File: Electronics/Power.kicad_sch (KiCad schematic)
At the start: 67 parts, among them IC1 TPS65251-1RHAR, IC2 MAX20008AFOC_VY+T, U6 AMS1117-3.3

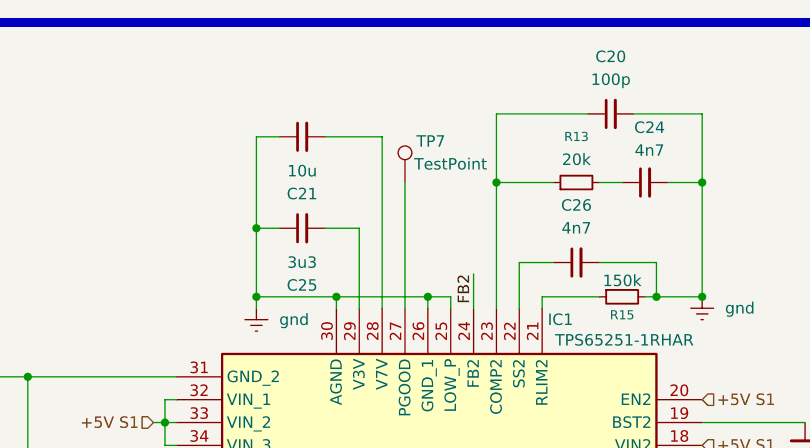
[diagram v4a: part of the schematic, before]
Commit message: Sata Port Changed
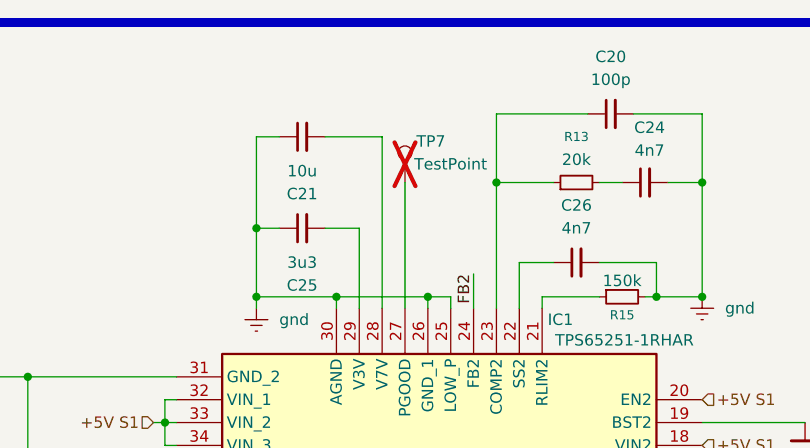
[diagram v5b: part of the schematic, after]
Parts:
- TP7: now not fitted; now left out of the parts list
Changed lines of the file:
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@@
 		(dnp no)
 		(fields_autoplaced yes)
-		(property "Reference" "#PWR050"
+		(property "Reference" "#PWR051"
 			(at 68.58 120.65 0)
 			(effects
@@
 			(project "CM5 Nas"
 				(path "/0650c7a8-acba-429c-9f8e-eec0baf0bc1c/fede4c36-00cc-4d3d-b71c-5243ba232202/588cd356-21c7-4636-b12c-e09ccb478c44"
-					(reference "#PWR050")
+					(reference "#PWR051")
 					(unit 1)
 				)
@@
 		(dnp no)
 		(fields_autoplaced yes)
-		(property "Reference" "#PWR040"
+		(property "Reference" "#PWR041"
 			(at 77.47 54.61 0)
 			(effects
@@
 			(project "CM5 Nas"
 				(path "/0650c7a8-acba-429c-9f8e-eec0baf0bc1c/fede4c36-00cc-4d3d-b71c-5243ba232202/588cd356-21c7-4636-b12c-e09ccb478c44"
-					(reference "#PWR040")
+					(reference "#PWR041")
 					(unit 1)
 				)
@@
 		(dnp no)
 		(fields_autoplaced yes)
-		(property "Reference" "#PWR043"
+		(property "Reference" "#PWR044"
 			(at 219.71 74.93 0)
 			(effects
@@
 			(project "CM5 Nas"
 				(path "/0650c7a8-acba-429c-9f8e-eec0baf0bc1c/fede4c36-00cc-4d3d-b71c-5243ba232202/588cd356-21c7-4636-b12c-e09ccb478c44"
-					(reference "#PWR043")
+					(reference "#PWR044")
 					(unit 1)
 				)
@@
 		(dnp no)
 		(fields_autoplaced yes)
-		(property "Reference" "#PWR039"
+		(property "Reference" "#PWR040"
 			(at 127 53.34 0)
 			(effects
@@
 			(project "CM5 Nas"
 				(path "/0650c7a8-acba-429c-9f8e-eec0baf0bc1c/fede4c36-00cc-4d3d-b71c-5243ba232202/588cd356-21c7-4636-b12c-e09ccb478c44"
-					(reference "#PWR039")
+					(reference "#PWR040")
 					(unit 1)
 				)
@@
 		(dnp no)
 		(fields_autoplaced yes)
-		(property "Reference" "#PWR041"
+		(property "Reference" "#PWR042"
 			(at 41.91 63.5 0)
 			(effects
@@
 			(project ""
 				(path "/0650c7a8-acba-429c-9f8e-eec0baf0bc1c/fede4c36-00cc-4d3d-b71c-5243ba232202/588cd356-21c7-4636-b12c-e09ccb478c44"
-					(reference "#PWR041")
+					(reference "#PWR042")
 					(unit 1)
 				)
@@
 		(dnp no)
 		(fields_autoplaced yes)
-		(property "Reference" "#PWR042"
+		(property "Reference" "#PWR043"
 			(at 152.4 50.8 0)
 			(effects
@@
 			(project "CM5 Nas"
 				(path "/0650c7a8-acba-429c-9f8e-eec0baf0bc1c/fede4c36-00cc-4d3d-b71c-5243ba232202/588cd356-21c7-4636-b12c-e09ccb478c44"
-					(reference "#PWR042")
+					(reference "#PWR043")
 					(unit 1)
 				)
@@
 		(on_board yes)
 		(dnp no)
-		(property "Reference" "#PWR051"
+		(property "Reference" "#PWR052"
 			(at 127 120.65 0)
 			(effects
@@
 			(project "CM5 Nas"
 				(path "/0650c7a8-acba-429c-9f8e-eec0baf0bc1c/fede4c36-00cc-4d3d-b71c-5243ba232202/588cd356-21c7-4636-b12c-e09ccb478c44"
-					(reference "#PWR051")
+					(reference "#PWR052")
 					(unit 1)
 				)
@@
 		(on_board yes)
 		(dnp no)
-		(property "Reference" "#PWR049"
+		(property "Reference" "#PWR050"
 			(at 251.46 109.22 0)
 			(effects
@@
 			(project "CM5 Nas"
 				(path "/0650c7a8-acba-429c-9f8e-eec0baf0bc1c/fede4c36-00cc-4d3d-b71c-5243ba232202/588cd356-21c7-4636-b12c-e09ccb478c44"
-					(reference "#PWR049")
+					(reference "#PWR050")
 					(unit 1)
 				)
@@
 		(dnp no)
 		(fields_autoplaced yes)
-		(property "Reference" "#PWR048"
+		(property "Reference" "#PWR049"
 			(at 99.06 107.95 0)
 			(effects
@@
 			(project "CM5 Nas"
 				(path "/0650c7a8-acba-429c-9f8e-eec0baf0bc1c/fede4c36-00cc-4d3d-b71c-5243ba232202/588cd356-21c7-4636-b12c-e09ccb478c44"
-					(reference "#PWR048")
+					(reference "#PWR049")
 					(unit 1)
 				)
@@
 		(dnp no)
 		(fields_autoplaced yes)
-		(property "Reference" "#PWR038"
+		(property "Reference" "#PWR039"
 			(at 165.1 30.48 0)
 			(effects
@@
 			(project "CM5 Nas"
 				(path "/0650c7a8-acba-429c-9f8e-eec0baf0bc1c/fede4c36-00cc-4d3d-b71c-5243ba232202/588cd356-21c7-4636-b12c-e09ccb478c44"
-					(reference "#PWR038")
+					(reference "#PWR039")
 					(unit 1)
 				)
@@
 		(on_board yes)
 		(dnp no)
-		(property "Reference" "#PWR0172"
+		(property "Reference" "#PWR035"
 			(at 29.21 31.75 0)
 			(effects
@@
 			(project "CM5 Nas"
 				(path "/0650c7a8-acba-429c-9f8e-eec0baf0bc1c/fede4c36-00cc-4d3d-b71c-5243ba232202/588cd356-21c7-4636-b12c-e09ccb478c44"
-					(reference "#PWR0172")
+					(reference "#PWR035")
 					(unit 1)
 				)
@@
 		(on_board yes)
 		(dnp no)
-		(property "Reference" "#PWR052"
+		(property "Reference" "#PWR053"
 			(at 226.06 128.27 0)
 			(effects
@@
 			(project "CM5 Nas"
 				(path "/0650c7a8-acba-429c-9f8e-eec0baf0bc1c/fede4c36-00cc-4d3d-b71c-5243ba232202/588cd356-21c7-4636-b12c-e09ccb478c44"
-					(reference "#PWR052")
+					(reference "#PWR053")
 					(unit 1)
 				)
@@
 		(unit 1)
 		(exclude_from_sim no)
-		(in_bom yes)
+		(in_bom no)
 		(on_board yes)
-		(dnp no)
+		(dnp yes)
 		(property "Reference" "TP7"
 			(at 95.25 29.718 0)
@@
 		(dnp no)
 		(fields_autoplaced yes)
-		(property "Reference" "#PWR046"
+		(property "Reference" "#PWR047"
 			(at 29.21 104.14 0)
 			(effects
@@
 			(project "CM5 Nas"
 				(path "/0650c7a8-acba-429c-9f8e-eec0baf0bc1c/fede4c36-00cc-4d3d-b71c-5243ba232202/588cd356-21c7-4636-b12c-e09ccb478c44"
-					(reference "#PWR046")
+					(reference "#PWR047")
 					(unit 1)
 				)
@@
 		(dnp no)
 		(fields_autoplaced yes)
-		(property "Reference" "#PWR045"
+		(property "Reference" "#PWR046"
 			(at 152.4 86.36 0)
 			(effects
@@
 			(project "CM5 Nas"
 				(path "/0650c7a8-acba-429c-9f8e-eec0baf0bc1c/fede4c36-00cc-4d3d-b71c-5243ba232202/588cd356-21c7-4636-b12c-e09ccb478c44"
-					(reference "#PWR045")
+					(reference "#PWR046")
 					(unit 1)
 				)
@@
 		(dnp no)
 		(fields_autoplaced yes)
-		(property "Reference" "#PWR047"
+		(property "Reference" "#PWR048"
 			(at 165.1 106.68 0)
 			(effects
@@
 			(project "CM5 Nas"
 				(path "/0650c7a8-acba-429c-9f8e-eec0baf0bc1c/fede4c36-00cc-4d3d-b71c-5243ba232202/588cd356-21c7-4636-b12c-e09ccb478c44"
-					(reference "#PWR047")
+					(reference "#PWR048")
 					(unit 1)
 				)
@@
 		(dnp no)
 		(fields_autoplaced yes)
-		(property "Reference" "#PWR044"
+		(property "Reference" "#PWR045"
 			(at 41.91 85.09 0)
 			(effects
@@
 			(project "CM5 Nas"
 				(path "/0650c7a8-acba-429c-9f8e-eec0baf0bc1c/fede4c36-00cc-4d3d-b71c-5243ba232202/588cd356-21c7-4636-b12c-e09ccb478c44"
-					(reference "#PWR044")
+					(reference "#PWR045")
 					(unit 1)
 				)
@@
 		(dnp no)
 		(fields_autoplaced yes)
-		(property "Reference" "#PWR036"
+		(property "Reference" "#PWR037"
 			(at 210.82 40.64 0)
 			(effects
@@
 			(project "CM5 Nas"
 				(path "/0650c7a8-acba-429c-9f8e-eec0baf0bc1c/fede4c36-00cc-4d3d-b71c-5243ba232202/588cd356-21c7-4636-b12c-e09ccb478c44"
-					(reference "#PWR036")
+					(reference "#PWR037")
 					(unit 1)
 				)
@@
 		(dnp no)
 		(fields_autoplaced yes)
-		(property "Reference" "#PWR035"
+		(property "Reference" "#PWR036"
 			(at 200.66 40.64 0)
 			(effects
@@
 			(project "CM5 Nas"
 				(path "/0650c7a8-acba-429c-9f8e-eec0baf0bc1c/fede4c36-00cc-4d3d-b71c-5243ba232202/588cd356-21c7-4636-b12c-e09ccb478c44"
-					(reference "#PWR035")
+					(reference "#PWR036")
 					(unit 1)
 				)
@@
 		(dnp no)
 		(fields_autoplaced yes)
-		(property "Reference" "#PWR037"
+		(property "Reference" "#PWR038"
 			(at 220.98 40.64 0)
 			(effects
@@
 			(project "CM5 Nas"
 				(path "/0650c7a8-acba-429c-9f8e-eec0baf0bc1c/fede4c36-00cc-4d3d-b71c-5243ba232202/588cd356-21c7-4636-b12c-e09ccb478c44"
-					(reference "#PWR037")
+					(reference "#PWR038")
 					(unit 1)
 				)

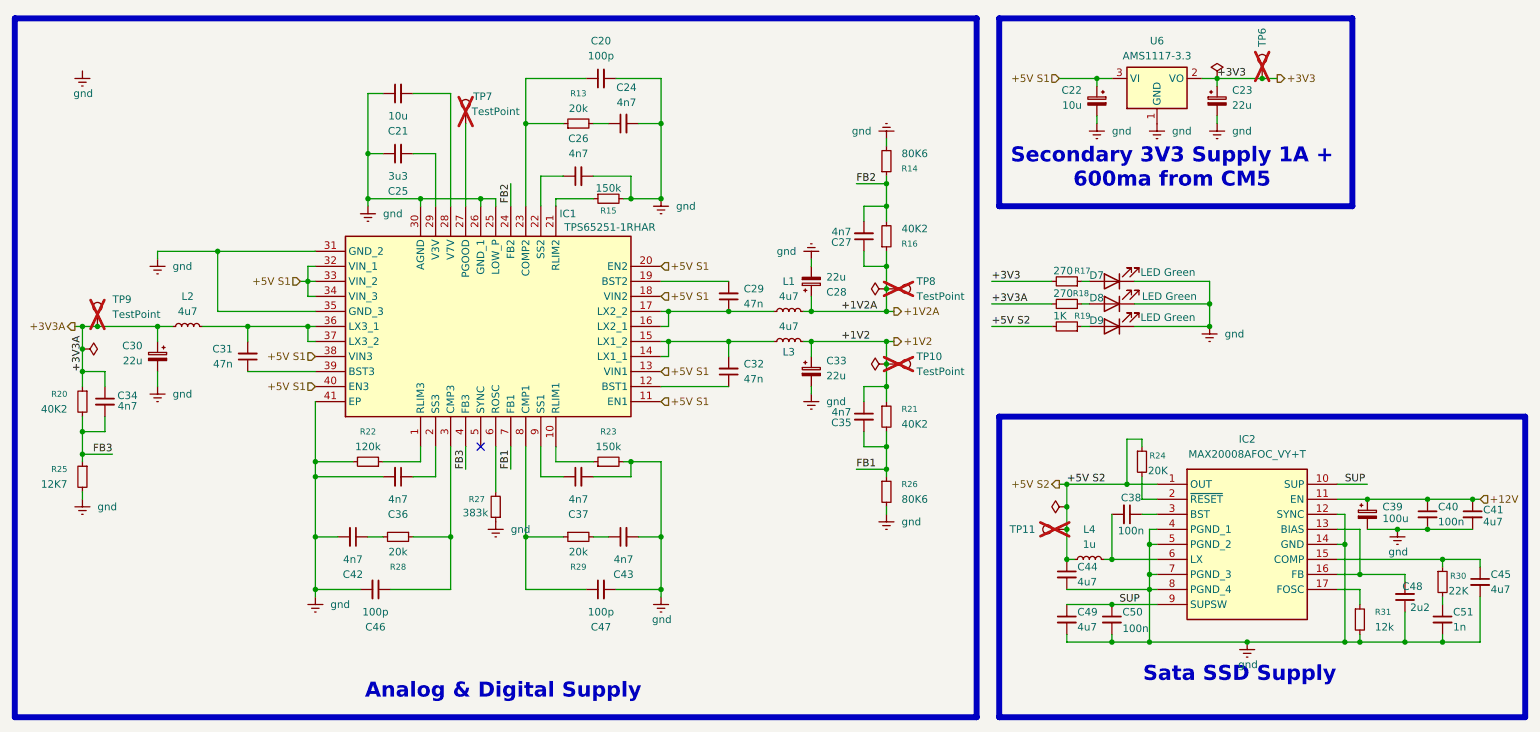
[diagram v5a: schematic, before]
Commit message: Changed sata port
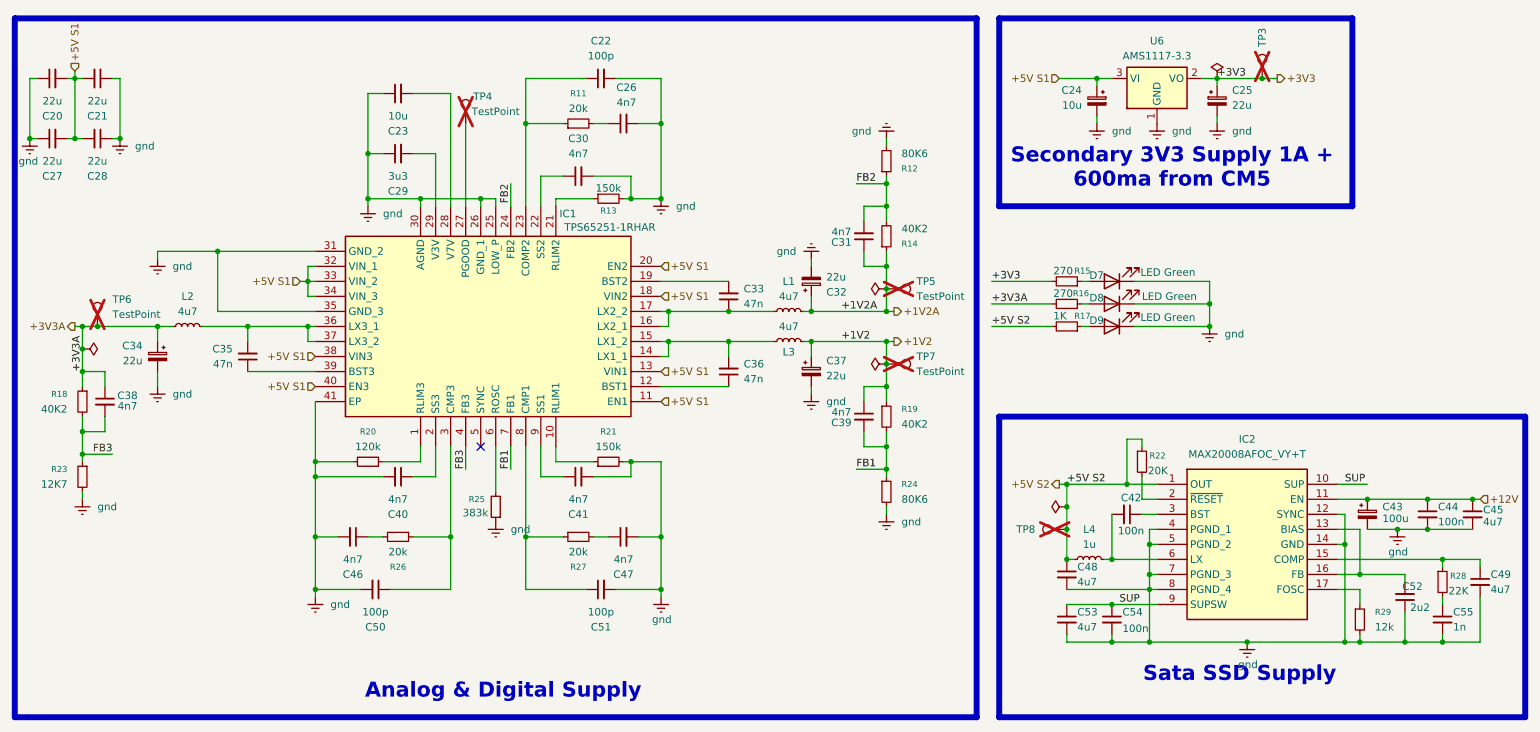
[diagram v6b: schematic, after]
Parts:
- added C20, C21, C27, C28: 22u, Capacitor_SMD:C_0805_2012Metric, symbol Device:C_Small
- IC1: footprint TPS65251-1RHAR:QFN50P600X600X100-41N-D -> Package_DFN_QFN:VQFN-40-1EP_6x6mm_P0.5mm_EP3.5x3.5mm_ThermalVias
- renumbered C20 to C22, C21 to C23, C22 to C24, C23 to C25, C24 to C26, C25 to C29, C26 to C30, C27 to C31, C28 to C32, C29 to C33, C30 to C34, C31 to C35, C32 to C36, C33 to C37, C34 to C38, C35 to C39, C36 to C40, C37 to C41, C38 to C42, C39 to C43, C40 to C44, C41 to C45, C42 to C46, C43 to C47, C44 to C48, C45 to C49, C46 to C50, C47 to C51, C48 to C52, C49 to C53, C50 to C54, C51 to C55, R13 to R11, R14 to R12, R15 to R13, R16 to R14, R17 to R15, R18 to R16, R19 to R17, R20 to R18, R21 to R19, R22 to R20, R23 to R21, R24 to R22, R25 to R23, R26 to R24, R27 to R25, R28 to R26, R29 to R27, R30 to R28, R31 to R29, TP6 to TP3, TP7 to TP4, TP8 to TP5, TP9 to TP6, TP10 to TP7, TP11 to TP8
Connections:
- net +5V S1: now also C20.2, C21.2, C27.2, C28.2
- net gnd: now also C20.1, C21.1, C27.1, C28.1

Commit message: More pcbing
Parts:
- removed C28: 22u, Capacitor_SMD:C_0805_2012Metric, symbol Device:C_Small
- C49, C53: footprint Capacitor_SMD:C_0805_2012Metric -> Capacitor_SMD:C_0402_1005Metric
- C52: footprint Capacitor_SMD:C_0603_1608Metric -> Capacitor_SMD:C_0402_1005Metric
- R18, R19, R23, R24, R25: footprint Resistor_SMD:R_0603_1608Metric -> Resistor_SMD:R_0402_1005Metric
- R28: footprint Resistor_SMD:R_0603_1608Metric -> Capacitor_SMD:C_0402_1005Metric
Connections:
- net SUP is gone; now on net +12V: C53.1, C54.1, IC2.10 (SUP), IC2.9 (SUPSW)

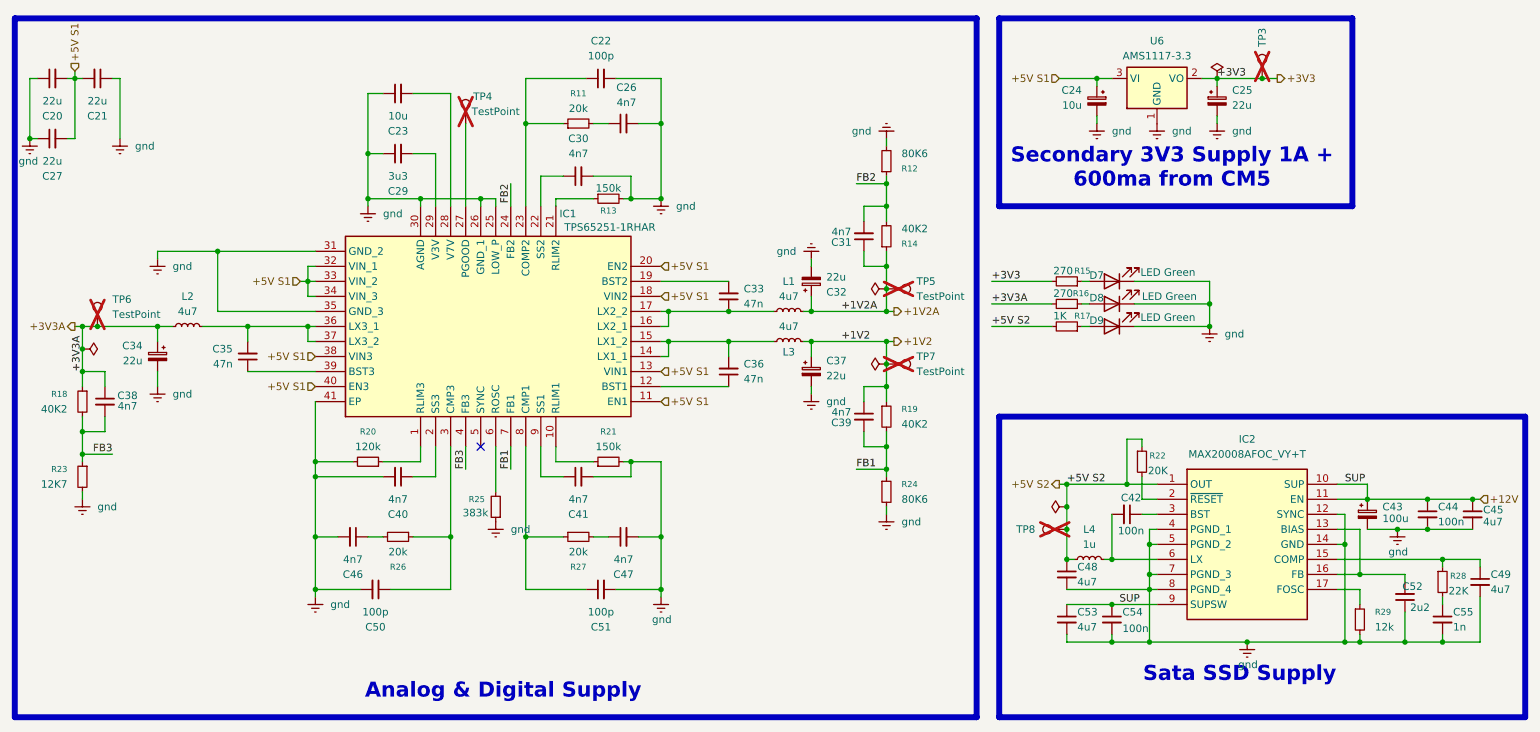
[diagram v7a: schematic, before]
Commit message: More pcb arangment, verticle ports
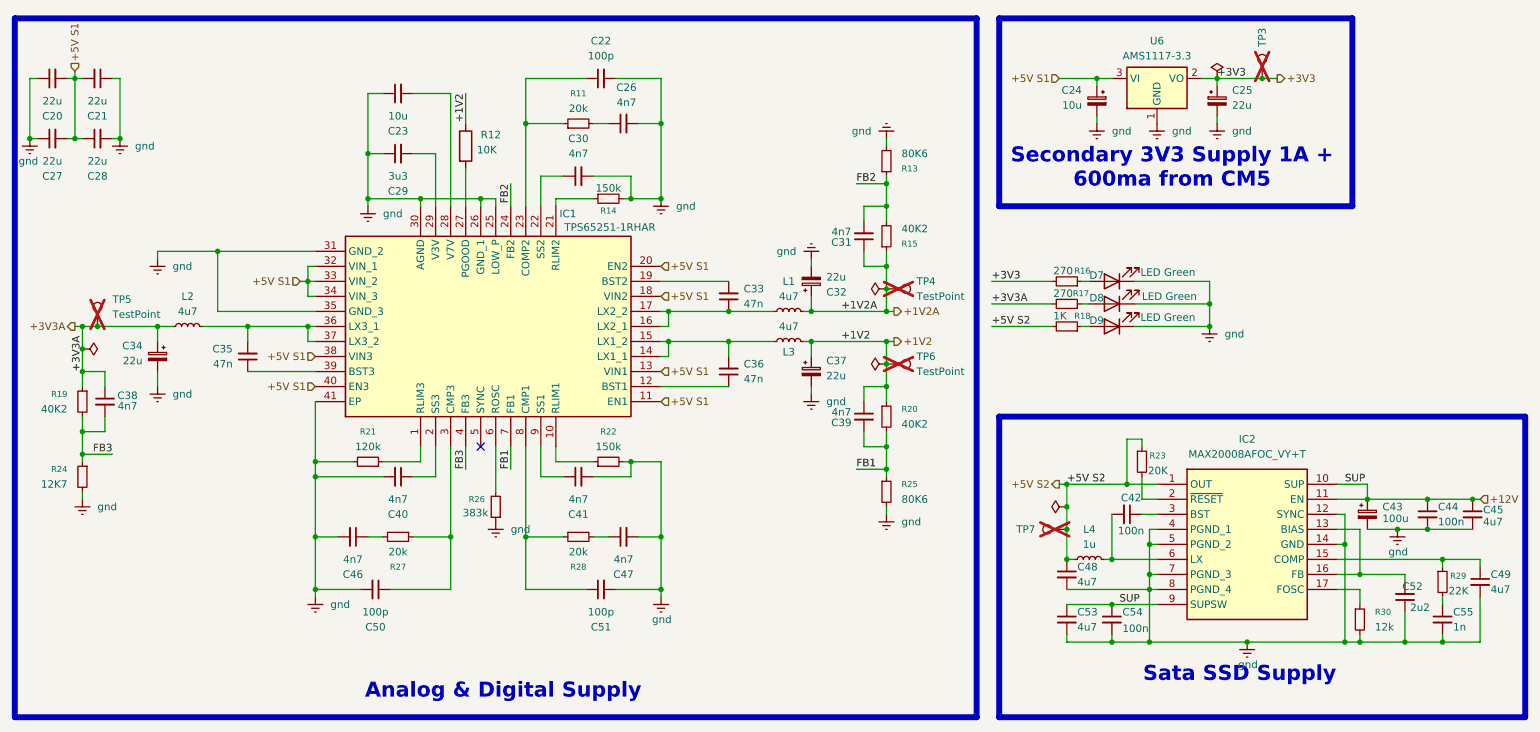
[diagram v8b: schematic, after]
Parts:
- removed TP4: TestPoint, TestPoint:TestPoint_Pad_1.0x1.0mm, symbol Connector:TestPoint
- added C28: 22u, Capacitor_SMD:C_0805_2012Metric, symbol Device:C_Small
- added R12: 10K, Resistor_SMD:R_0603_1608Metric, symbol Device:R
- C23, C29: footprint Capacitor_SMD:C_0805_2012Metric -> Capacitor_SMD:C_0603_1608Metric
- R11: footprint Resistor_SMD:R_0603_1608Metric -> Resistor_SMD:R_0402_1005Metric
- R13: renamed from R12; footprint Resistor_SMD:R_0603_1608Metric -> Resistor_SMD:R_0402_1005Metric
- R14: renamed from R13; footprint Resistor_SMD:R_0603_1608Metric -> Resistor_SMD:R_0402_1005Metric
- R15: renamed from R14; footprint Resistor_SMD:R_0603_1608Metric -> Resistor_SMD:R_0402_1005Metric
- renumbered R15 to R16, R16 to R17, R17 to R18, R18 to R19, R19 to R20, R20 to R21, R21 to R22, R22 to R23, R23 to R24, R24 to R25, R25 to R26, R26 to R27, R27 to R28, R28 to R29, R29 to R30, TP5 to TP4, TP6 to TP5, TP7 to TP6, TP8 to TP7
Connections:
- net +1V2: now also R12.1
- net +5V S1: now also C28.1
- net gnd: now also C28.2
- net at IC1.27 (PGOOD): now also R12.2
